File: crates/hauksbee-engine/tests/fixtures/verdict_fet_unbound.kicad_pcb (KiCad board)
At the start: 3 parts, among them Q1 XFET9999

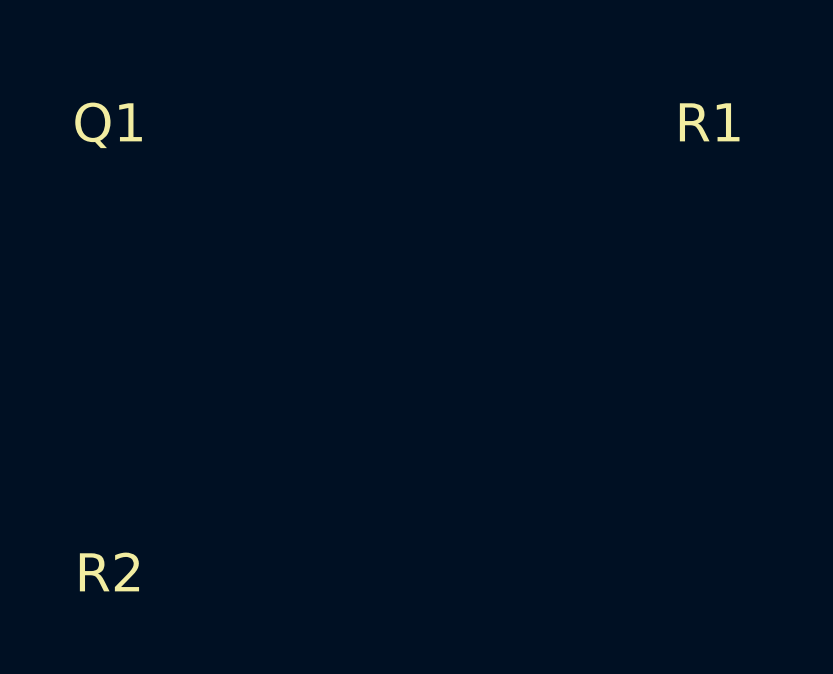
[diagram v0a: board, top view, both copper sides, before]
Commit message: Report unrouted pads and layouts out of date with their schematic
Copper connectivity (drc/connectivity.rs) reuses the short sweep's primitives
and R-tree to union same-net pads, tracks, arcs, vias, filled zones and net
graphics layer by layer; a net split into islands has a pad copper never
reaches (KiCad's unconnected items). Plated through-hole pads join every
copper layer, net-tie and jumper pad groups join their pads, NPTH, no-connect
and netless pads are never required, unfilled zones are named once rather
than judged, and a layout with no routing at all is one note.

When a same-stem schematic sits beside the layout, the pin-by-pin net
partitions are compared (names ignored, unfitted and one-sided parts counted
and skipped) and each group of moved pins is one finding.

The schematic reader now needs a junction for a wire ending on another
wire's interior, and takes a reused sheet's unit per placement, both checked
against kicad-cli netlists.
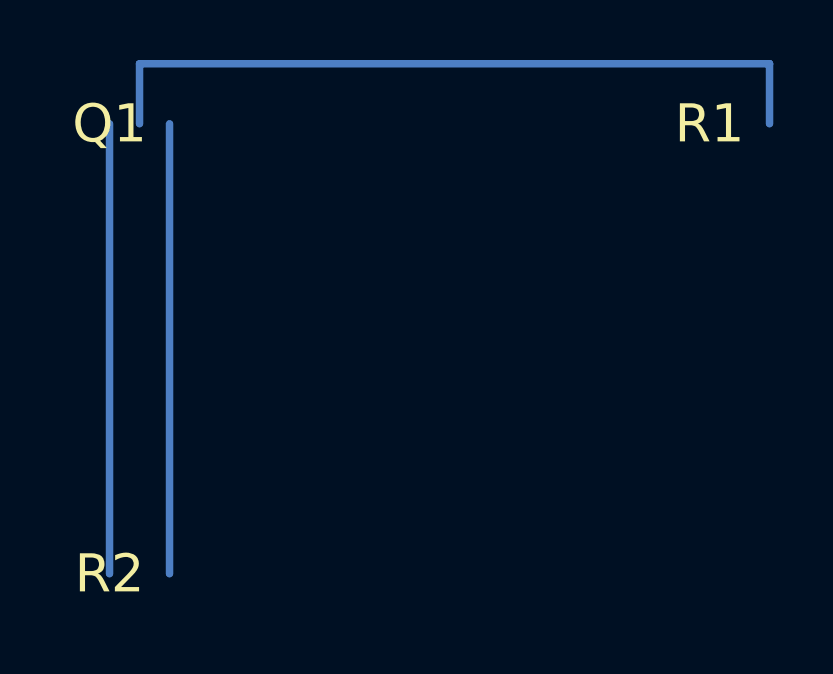
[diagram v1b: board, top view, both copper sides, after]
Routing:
- net LOAD_DRAIN: track 0.00 -> 25.0 mm
- net GND: track 0.00 -> 15.0 mm
- net GATE_CTRL: track 0.00 -> 15.0 mm
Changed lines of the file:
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@@
     (pad 2 thru_hole circle (at 2 0) (net 1 "GND"))
   )
+  (segment (start 110 100) (end 110 115) (width 0.25) (layer B.Cu) (net 3))
+  (segment (start 112 100) (end 112 115) (width 0.25) (layer B.Cu) (net 1))
+  (segment (start 111 100) (end 111 98) (width 0.25) (layer B.Cu) (net 4))
+  (segment (start 111 98) (end 132 98) (width 0.25) (layer B.Cu) (net 4))
+  (segment (start 132 98) (end 132 100) (width 0.25) (layer B.Cu) (net 4))
 )
